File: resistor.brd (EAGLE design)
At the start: 10.2 x 39.5 mm, 3 parts

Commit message: New Updates
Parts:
- moved U$2 0.28 mm to (11.2, 36.4)
- moved U$1 0.25 mm to (11.3, 11.0)
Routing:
- net N$1: track 7.11 -> 6.25 mm
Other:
- board size 10.2 x 39.5 mm -> 14.5 x 39.5 mm
- board text added: "care@Pinwheel.in"
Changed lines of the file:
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@@
 <setting verticaltext="up"/>
 </settings>
-<grid distance="50" unitdist="mil" unit="mm" style="lines" multiple="1" display="yes" altdistance="5" altunitdist="mil" altunit="mm"/>
+<grid distance="0.5" unitdist="mm" unit="mm" style="lines" multiple="1" display="yes" altdistance="5" altunitdist="mil" altunit="mm"/>
 <layers>
 <layer number="1" name="Top" color="4" fill="1" visible="yes" active="yes"/>
@@
 <layer number="43" name="vRestrict" color="2" fill="10" visible="yes" active="yes"/>
 <layer number="44" name="Drills" color="7" fill="1" visible="no" active="yes"/>
-<layer number="45" name="Holes" color="7" fill="1" visible="no" active="yes"/>
+<layer number="45" name="Holes" color="7" fill="1" visible="yes" active="yes"/>
 <layer number="46" name="Milling" color="3" fill="1" visible="no" active="yes"/>
 <layer number="47" name="Measures" color="7" fill="1" visible="no" active="yes"/>
@@
 <board>
 <plain>
-<wire x1="6.35" y1="3.81" x2="16.5" y2="3.81" width="0" layer="20"/>
-<wire x1="16.5" y1="3.81" x2="16.5" y2="43.307" width="0" layer="20"/>
-<wire x1="16.5" y1="43.307" x2="6.35" y2="43.297" width="0" layer="20"/>
-<wire x1="6.35" y1="43.297" x2="6.35" y2="3.81" width="0" layer="20"/>
-<text x="15.494" y="20.32" size="0.8128" layer="21" rot="R90">Pinwheel Robotics </text>
+<wire x1="4" y1="41.7659" x2="4" y2="5.683746875" width="0" layer="20"/>
+<wire x1="4" y1="5.683746875" x2="5.683746875" y2="4" width="0" layer="20" curve="90"/>
+<wire x1="5.683746875" y1="4" x2="16.731853125" y2="4" width="0" layer="20"/>
+<wire x1="16.731853125" y1="4" x2="18.5" y2="5.768146875" width="0" layer="20" curve="90"/>
+<wire x1="18.5" y1="5.768146875" x2="18.5" y2="41.728584375" width="0" layer="20"/>
+<wire x1="18.5" y1="41.728584375" x2="16.728584375" y2="43.5" width="0" layer="20" curve="90"/>
+<wire x1="16.728584375" y1="43.5" x2="5.7341" y2="43.5" width="0" layer="20"/>
+<wire x1="5.7341" y1="43.5" x2="4" y2="41.7659" width="0" layer="20" curve="90"/>
+<hole x="6" y="41.5" drill="3"/>
+<hole x="16.5" y="41.5" drill="3"/>
+<hole x="6" y="6" drill="3"/>
+<hole x="16.5" y="6" drill="3"/>
+<text x="17.5" y="12.5" size="1.778" layer="21" rot="R90">Pinwheel Robotics</text>
+<text x="6.858" y="34.036" size="1.778" layer="22" rot="MR270">care@Pinwheel.in</text>
 </plain>
 <attributes>
@@
 <attribute name="VALUE" x="12.065" y="19.177" size="1.27" layer="27" ratio="10" rot="R90"/>
 </element>
-<element name="U$2" library="microbit" package="MICROBIT_PAD" value="MICROBIT_PAD" x="11.43" y="36.195" smashed="yes" rot="R180">
-<attribute name="NAME" x="11.303" y="42.418" size="1.27" layer="21" rot="R270"/>
+<element name="U$2" library="microbit" package="MICROBIT_PAD" value="MICROBIT_PAD" x="11.246" y="36.4" smashed="yes" rot="R180">
+<attribute name="NAME" x="11.119" y="42.623" size="1.27" layer="21" rot="R270"/>
 </element>
-<element name="U$1" library="microbit" package="MICROBIT_PAD" value="MICROBIT_PAD" x="11.557" y="11.049" smashed="yes">
-<attribute name="NAME" x="12.7" y="4.953" size="1.27" layer="21" rot="R90"/>
+<element name="U$1" library="microbit" package="MICROBIT_PAD" value="MICROBIT_PAD" x="11.303" y="11.049" smashed="yes">
+<attribute name="NAME" x="12.446" y="4.953" size="1.27" layer="21" rot="R90"/>
 </element>
 </elements>
@@
 <contactref element="R1" pad="1"/>
 <contactref element="U$1" pad="PAD"/>
-<wire x1="11.43" y1="17.272" x2="11.43" y2="10.16" width="2.54" layer="16"/>
-<wire x1="11.43" y1="10.16" x2="11.557" y2="11.049" width="0" layer="19" extent="16-16"/>
+<wire x1="11.43" y1="17.272" x2="11.43" y2="11.35560625" width="0.508" layer="16"/>
+<wire x1="11.43" y1="11.35560625" x2="11.303" y2="11.049" width="0.508" layer="16" curve="-45"/>
 </signal>
 <signal name="N$2">
 <contactref element="U$2" pad="PAD"/>
 <contactref element="R1" pad="2"/>
-<wire x1="11.43" y1="36.195" x2="11.43" y2="29.972" width="2.54" layer="16"/>
+<wire x1="11.43" y1="29.972" x2="11.43" y2="35.7228625" width="0.508" layer="16"/>
+<wire x1="11.43" y1="35.7228625" x2="11.246" y2="36.4" width="0.508" layer="16" curve="45"/>
 </signal>
 </signals>

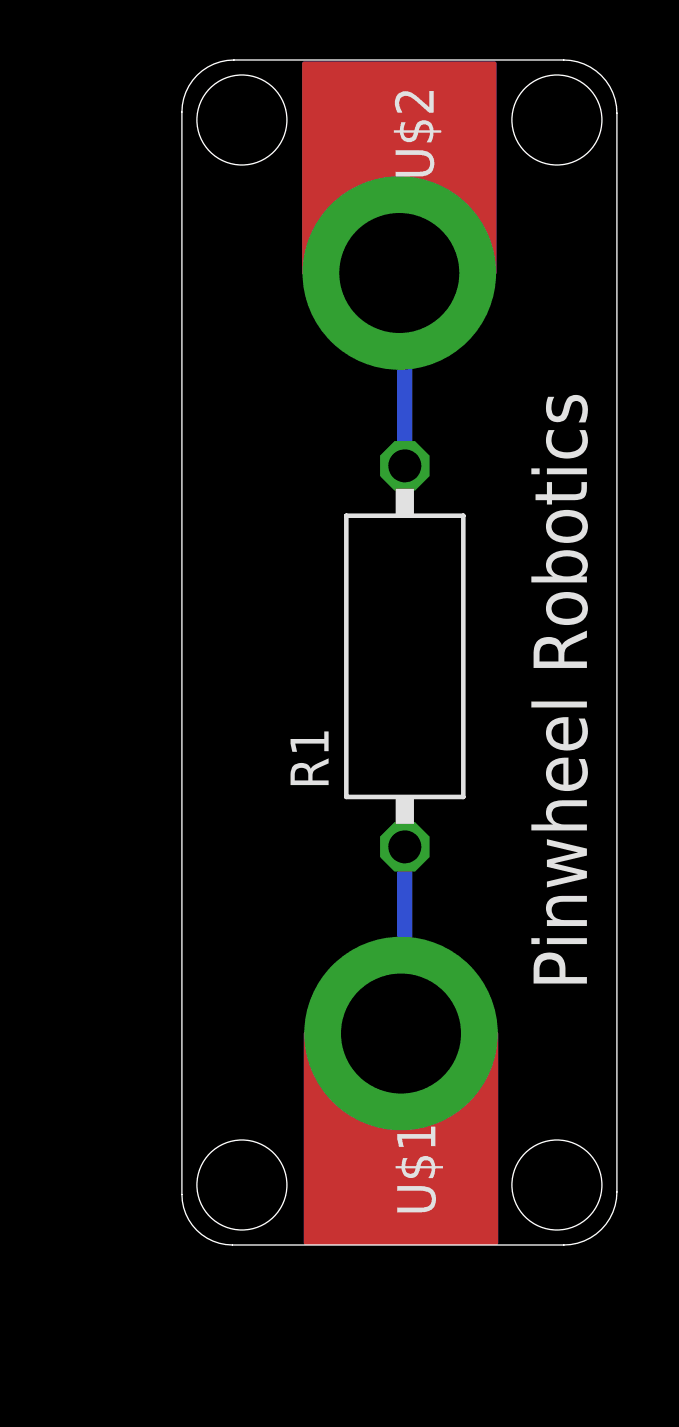
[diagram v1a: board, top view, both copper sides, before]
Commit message: New Update for board curv
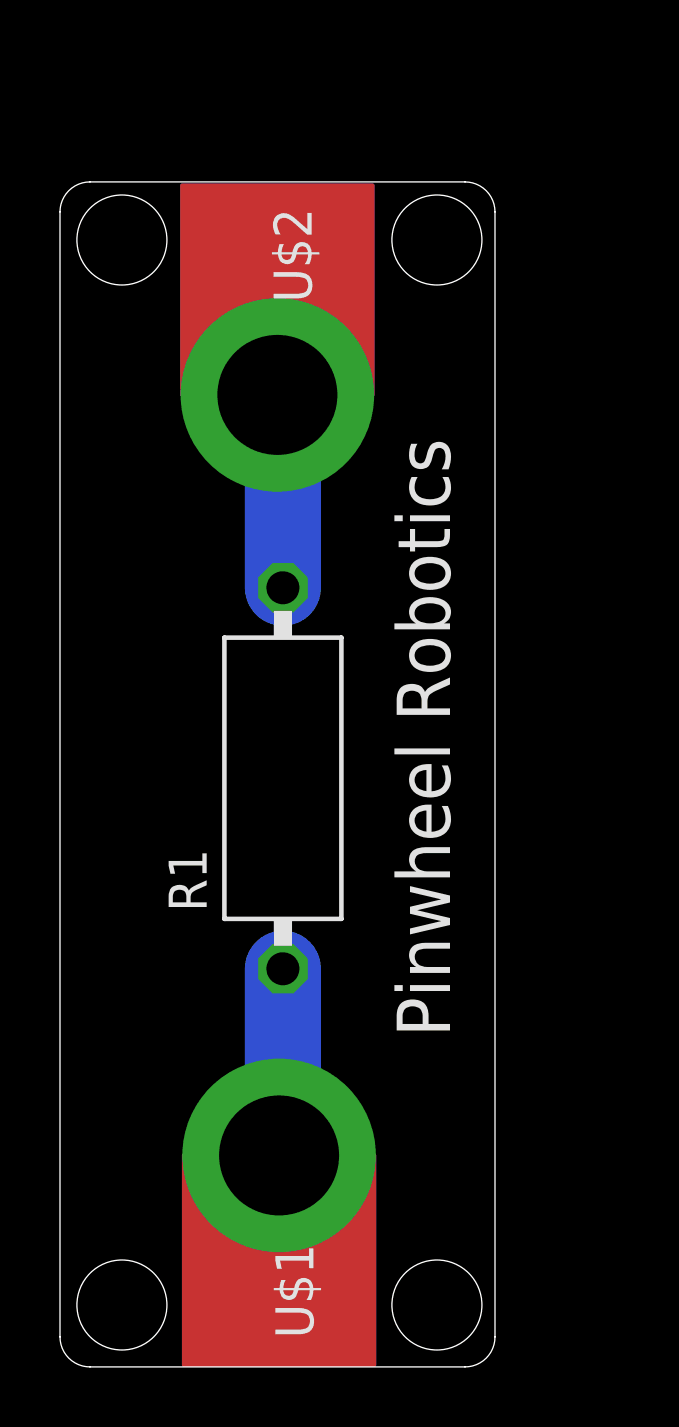
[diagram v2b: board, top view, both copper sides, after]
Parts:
- moved R1 5.75 mm to (7.37, 19.6)
- moved U$1 5.75 mm to (7.24, 6.99)
- moved U$2 5.75 mm to (7.18, 32.3)
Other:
- outline, holes or cut-outs redrawn
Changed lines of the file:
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@@
 <board>
 <plain>
-<wire x1="4" y1="41.7659" x2="4" y2="5.683746875" width="0" layer="20"/>
-<wire x1="4" y1="5.683746875" x2="5.683746875" y2="4" width="0" layer="20" curve="90"/>
-<wire x1="5.683746875" y1="4" x2="16.731853125" y2="4" width="0" layer="20"/>
-<wire x1="16.731853125" y1="4" x2="18.5" y2="5.768146875" width="0" layer="20" curve="90"/>
-<wire x1="18.5" y1="5.768146875" x2="18.5" y2="41.728584375" width="0" layer="20"/>
-<wire x1="18.5" y1="41.728584375" x2="16.728584375" y2="43.5" width="0" layer="20" curve="90"/>
-<wire x1="16.728584375" y1="43.5" x2="5.7341" y2="43.5" width="0" layer="20"/>
-<wire x1="5.7341" y1="43.5" x2="4" y2="41.7659" width="0" layer="20" curve="90"/>
-<hole x="6" y="41.5" drill="3"/>
-<hole x="16.5" y="41.5" drill="3"/>
-<hole x="6" y="6" drill="3"/>
-<hole x="16.5" y="6" drill="3"/>
-<text x="17.5" y="12.5" size="1.778" layer="21" rot="R90">Pinwheel Robotics</text>
-<text x="6.858" y="34.036" size="1.778" layer="22" rot="MR270">care@Pinwheel.in</text>
+<wire x1="-0.064" y1="38.436" x2="-0.064" y2="0.936" width="0" layer="20"/>
+<wire x1="-0.064" y1="0.936" x2="0.936" y2="-0.064" width="0" layer="20" curve="90"/>
+<wire x1="0.936" y1="-0.064" x2="13.436" y2="-0.064" width="0" layer="20"/>
+<wire x1="13.436" y1="-0.064" x2="14.436" y2="0.936" width="0" layer="20" curve="90"/>
+<wire x1="14.436" y1="0.936" x2="14.436" y2="38.436" width="0" layer="20"/>
+<wire x1="14.436" y1="38.436" x2="13.436" y2="39.436" width="0" layer="20" curve="90"/>
+<wire x1="13.436" y1="39.436" x2="0.936" y2="39.436" width="0" layer="20"/>
+<wire x1="0.936" y1="39.436" x2="-0.064" y2="38.436" width="0" layer="20" curve="90"/>
+<hole x="2" y="37.5" drill="3"/>
+<hole x="12.5" y="37.5" drill="3"/>
+<hole x="2" y="2" drill="3"/>
+<hole x="12.5" y="2" drill="3"/>
+<text x="12.936" y="10.936" size="1.778" layer="21" rot="R90">Pinwheel Robotics</text>
+<text x="2.794" y="29.972" size="1.778" layer="22" rot="MR270">care@Pinwheel.in</text>
 </plain>
 <attributes>
@@
 </autorouter>
 <elements>
-<element name="R1" library="rcl" library_urn="urn:adsk.eagle:library:334" package="VMTB60" package3d_urn="urn:adsk.eagle:package:26122/2" value="" x="11.43" y="23.622" smashed="yes" rot="R90">
-<attribute name="NAME" x="8.89" y="19.177" size="1.27" layer="25" ratio="10" rot="R90"/>
-<attribute name="POPULARITY" value="0" x="29.21" y="43.942" size="1.778" layer="27" rot="R90" display="off"/>
-<attribute name="SPICEPREFIX" value="R" x="29.21" y="43.942" size="1.778" layer="27" rot="R90" display="off"/>
-<attribute name="VALUE" x="12.065" y="19.177" size="1.27" layer="27" ratio="10" rot="R90"/>
+<element name="R1" library="rcl" library_urn="urn:adsk.eagle:library:334" package="VMTB60" package3d_urn="urn:adsk.eagle:package:26122/2" value="" x="7.366" y="19.558" smashed="yes" rot="R90">
+<attribute name="NAME" x="4.826" y="15.113" size="1.27" layer="25" ratio="10" rot="R90"/>
+<attribute name="POPULARITY" value="0" x="25.146" y="39.878" size="1.778" layer="27" rot="R90" display="off"/>
+<attribute name="SPICEPREFIX" value="R" x="25.146" y="39.878" size="1.778" layer="27" rot="R90" display="off"/>
+<attribute name="VALUE" x="8.001" y="15.113" size="1.27" layer="27" ratio="10" rot="R90"/>
 </element>
-<element name="U$2" library="microbit" package="MICROBIT_PAD" value="MICROBIT_PAD" x="11.246" y="36.4" smashed="yes" rot="R180">
-<attribute name="NAME" x="11.119" y="42.623" size="1.27" layer="21" rot="R270"/>
+<element name="U$2" library="microbit" package="MICROBIT_PAD" value="MICROBIT_PAD" x="7.182" y="32.336" smashed="yes" rot="R180">
+<attribute name="NAME" x="7.055" y="38.559" size="1.27" layer="21" rot="R270"/>
 </element>
-<element name="U$1" library="microbit" package="MICROBIT_PAD" value="MICROBIT_PAD" x="11.303" y="11.049" smashed="yes">
-<attribute name="NAME" x="12.446" y="4.953" size="1.27" layer="21" rot="R90"/>
+<element name="U$1" library="microbit" package="MICROBIT_PAD" value="MICROBIT_PAD" x="7.239" y="6.985" smashed="yes">
+<attribute name="NAME" x="8.382" y="0.889" size="1.27" layer="21" rot="R90"/>
 </element>
 </elements>
@@
 <contactref element="R1" pad="1"/>
 <contactref element="U$1" pad="PAD"/>
-<wire x1="11.43" y1="17.272" x2="11.43" y2="11.35560625" width="0.508" layer="16"/>
-<wire x1="11.43" y1="11.35560625" x2="11.303" y2="11.049" width="0.508" layer="16" curve="-45"/>
+<wire x1="7.366" y1="13.208" x2="7.366" y2="7.29160625" width="2.54" layer="16"/>
+<wire x1="7.366" y1="7.29160625" x2="7.239" y2="6.985" width="0.508" layer="16" curve="-45"/>
 </signal>
 <signal name="N$2">
 <contactref element="U$2" pad="PAD"/>
 <contactref element="R1" pad="2"/>
-<wire x1="11.43" y1="29.972" x2="11.43" y2="35.7228625" width="0.508" layer="16"/>
-<wire x1="11.43" y1="35.7228625" x2="11.246" y2="36.4" width="0.508" layer="16" curve="45"/>
+<wire x1="7.366" y1="25.908" x2="7.366" y2="31.6588625" width="2.54" layer="16"/>
+<wire x1="7.366" y1="31.6588625" x2="7.182" y2="32.336" width="0.508" layer="16" curve="45"/>
 </signal>
 </signals>
